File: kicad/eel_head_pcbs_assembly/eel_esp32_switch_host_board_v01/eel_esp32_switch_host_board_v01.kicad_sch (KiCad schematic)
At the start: 19 parts, among them J1 Conn_01x02_Female, J2 motor_l, J3 motor_r, J4 neopixels, J5 n00ds, U1 XIAO-ESP32C3, U2 DRV8833, U3 ep2_txco_rx, U4 5v_0.6a_boost_converter, U5 FMBM5551, U6 FMBM5551

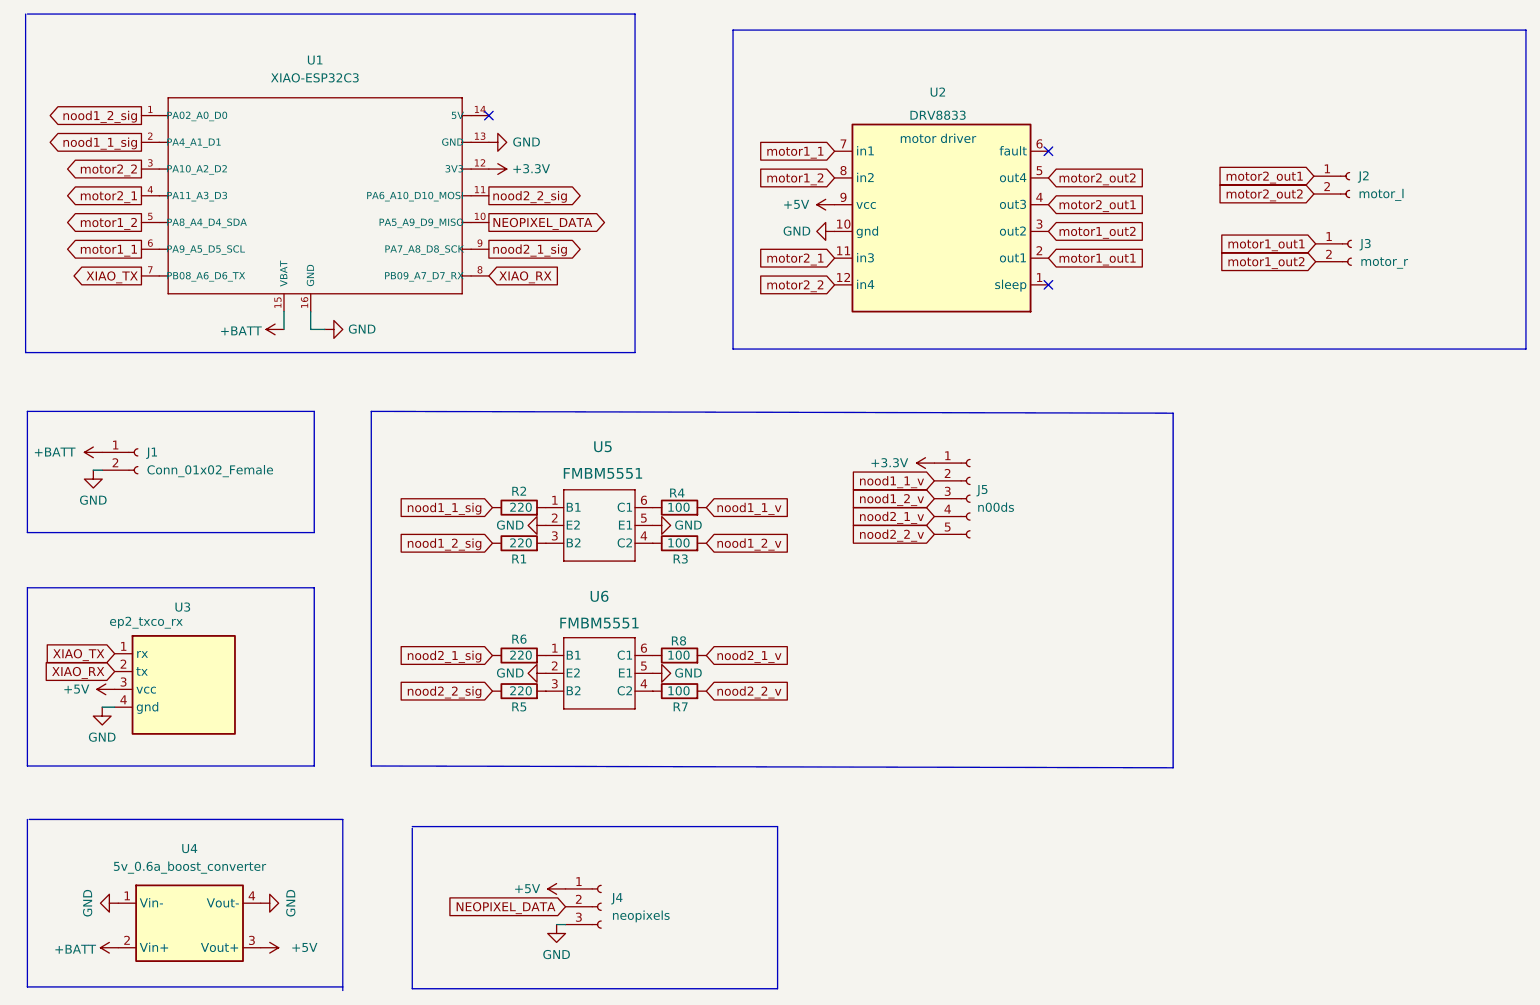
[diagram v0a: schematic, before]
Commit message: create pcb just for esp32 and on/off switch
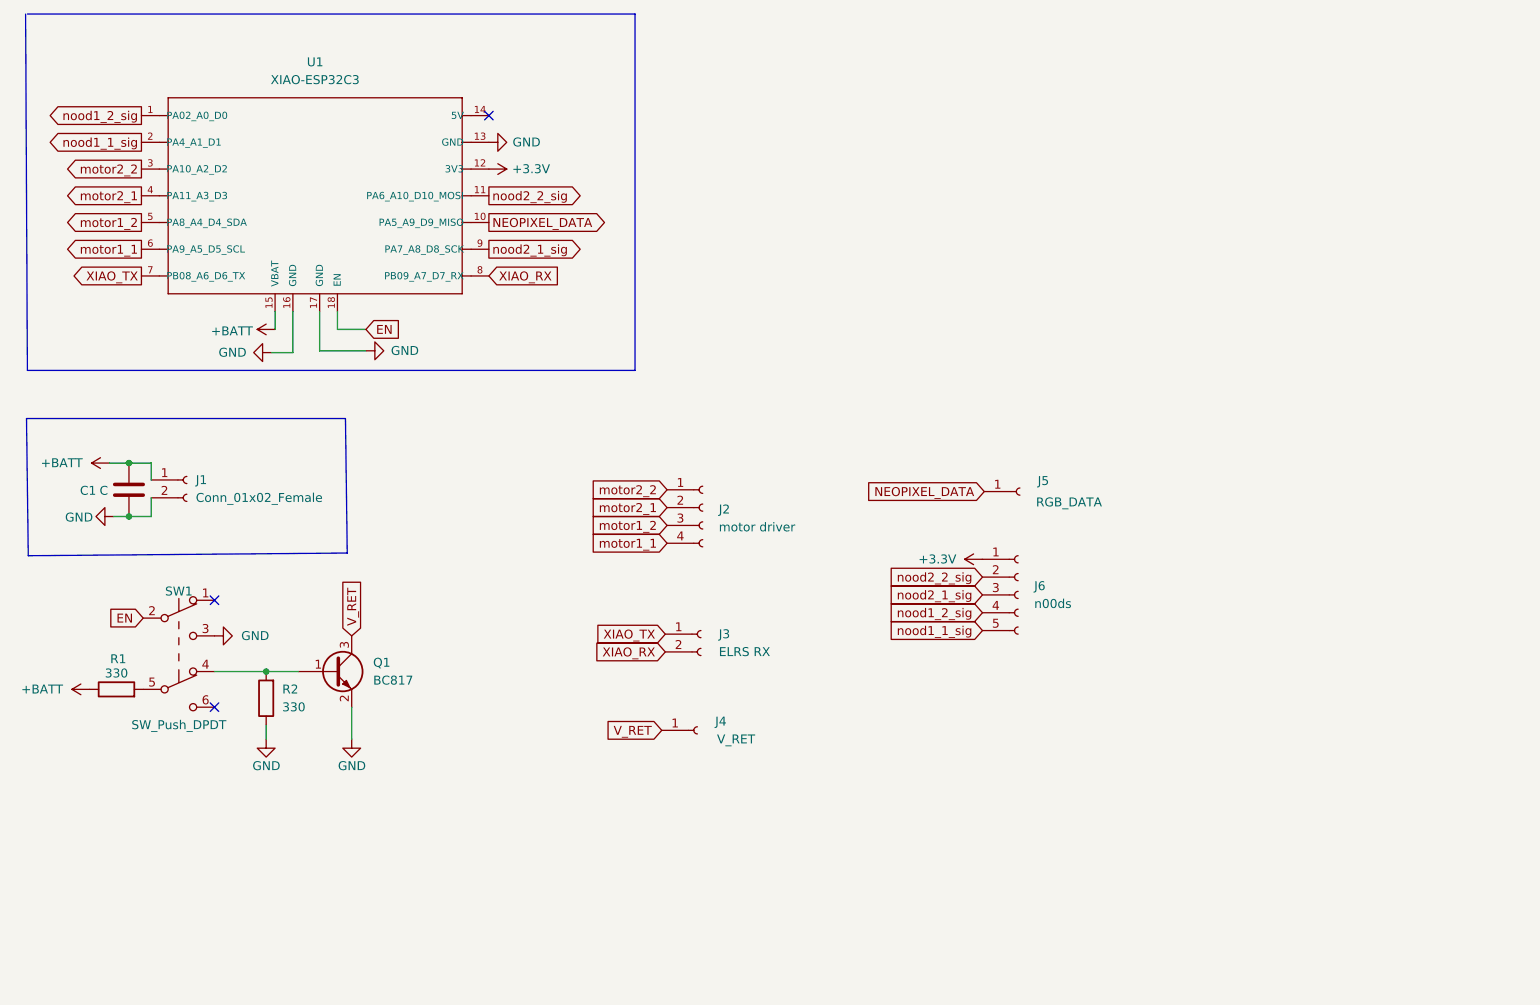
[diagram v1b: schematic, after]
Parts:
- removed J2: motor_l, haribo_kimchi_boards:smd_solder_pads_1x02_2.54mm, symbol Connector:Conn_01x02_Female
- removed J4: neopixels, haribo_kimchi_boards:smd_solder_pads_1x03_2.54mm, symbol Connector:Conn_01x03_Female
- removed R3, R4, R7, R8: 100, Resistor_SMD:R_0603_1608Metric_Pad0.98x0.95mm_HandSolder, symbol Device:R
- removed R5, R6: 220, Resistor_SMD:R_0603_1608Metric_Pad0.98x0.95mm_HandSolder, symbol Device:R
- removed U2: DRV8833, haribo_kimchi_boards:drv8833_breakout, symbol haribo_kimchi_boards:DRV8833_breakout
- removed U3: ep2_txco_rx, haribo_kimchi_boards:happymodel_ep2_txco_rx, symbol haribo_kimchi_boards:happymodel_ep1_txco_rx
- removed U4: 5v_0.6a_boost_converter, haribo_kimchi_boards:5v_0.6a_boost_converter, symbol haribo_kimchi_boards:5v_0.6a_boost_converter
- removed U5, U6: FMBM5551, haribo_kimchi_extra_footprints:SSOT6_3X1P7_ONS, symbol onsemi_FMBM5551:FMBM5551
- added C1: C, Capacitor_SMD:C_0805_2012Metric_Pad1.18x1.45mm_HandSolder, symbol Device:C
- added J2: motor driver, haribo_kimchi_boards:smd_solder_pads_1x04, symbol Connector:Conn_01x04_Female
- added J4: V_RET, haribo_kimchi_boards:smd_solder_pads_1x01_2.54mm, symbol Connector:Conn_01x01_Female
- added J5: RGB_DATA, haribo_kimchi_boards:smd_solder_pads_1x01_2.54mm, symbol Connector:Conn_01x01_Female
- added Q1: BC817, Package_TO_SOT_SMD:SOT-23, symbol Transistor_BJT:BC817
- added SW1: SW_Push_DPDT, haribo_kimchi_extra_footprints:Nidec_2x03_dpdt_CL-SB-22B-11, symbol Switch:SW_Push_DPDT
- J1: footprint Connector_JST:JST_PH_S2B-PH-K_1x02_P2.00mm_Horizontal -> haribo_kimchi_boards:smd_solder_pads_1x02_2.54mm
- J3: value motor_r -> ELRS RX
- J6: renamed from J5; footprint haribo_kimchi_boards:smd_solder_pads_1x05_n00ds_v2_smaller -> haribo_kimchi_boards:smd_solder_pads_1x05_n00ds_v3_smaller
- R1, R2: value 220 -> 330; footprint Resistor_SMD:R_0603_1608Metric_Pad0.98x0.95mm_HandSolder -> Resistor_SMD:R_0805_2012Metric_Pad1.20x1.40mm_HandSolder; Vendor C22962 -> (none)
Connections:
- net motor1_out1 is gone; now on net XIAO_TX: J3.1 (Pin_1)
- net motor1_out2 is gone; now on net XIAO_RX: J3.2 (Pin_2)
- net nood1_1_v is gone; now on net nood2_2_sig: J6.2 (Pin_2)
- net nood1_2_v is gone; now on net nood2_1_sig: J6.3 (Pin_3)
- net nood2_1_v is gone; now on net nood1_2_sig: J6.4 (Pin_4)
- net nood2_2_v is gone; now on net nood1_1_sig: J6.5 (Pin_5)
- net +BATT: now also R1.1, C1.1
- net GND: now also R2.1, U1.17 (GND), C1.2, Q1.2 (E), SW1.3 (C)
- net NEOPIXEL_DATA: now also J5.1 (Pin_1)
- net motor1_1: now also J2.4 (Pin_4)
- net motor1_2: now also J2.3 (Pin_3)
- net motor2_1: now also J2.2 (Pin_2)
- net motor2_2: now also J2.1 (Pin_1)
- net nood1_1_sig: no longer R2.1
- net nood1_2_sig: no longer R1.1
- net at R2.2: now also Q1.1 (B), SW1.4 (A)
- net at R1.2: now also SW1.5 (B)
- new net EN: SW1.2 (B), U1.18 (EN)
- new net V_RET: J4.1 (Pin_1), Q1.3 (C)
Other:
- moved on the sheet: J1, J6

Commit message: final touches initial pcb design
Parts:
- R2: value 330 -> 1k
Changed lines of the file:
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@@
       (effects (font (size 1.27 1.27)) (justify right))
     )
-    (property "Value" "330" (id 1) (at 58.674 118.6179 0)
+    (property "Value" "1k" (id 1) (at 58.674 118.6179 0)
       (effects (font (size 1.27 1.27)) (justify right))
     )
@@
     )
     (path "/56e09bd3-3867-4668-b547-93b60558f9f0"
-      (reference "R2") (unit 1) (value "330") (footprint "Resistor_SMD:R_0805_2012Metric_Pad1.20x1.40mm_HandSolder")
+      (reference "R2") (unit 1) (value "1k") (footprint "Resistor_SMD:R_0805_2012Metric_Pad1.20x1.40mm_HandSolder")
     )
     (path "/609ab77a-7732-4674-8d1a-d72669237dfa"
